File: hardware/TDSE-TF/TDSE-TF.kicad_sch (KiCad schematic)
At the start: 38 parts, among them J1 Sensor nivel de agua, J10 CN10, J11 220VCA salida, J2 Tira LED, J3 +5VCC entrada, J4 220VCA entrada, J5 Bomba, J6 Sensor nivel de luz, J7 Conector LCD16x02, J8 Sensor humedad de suelo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

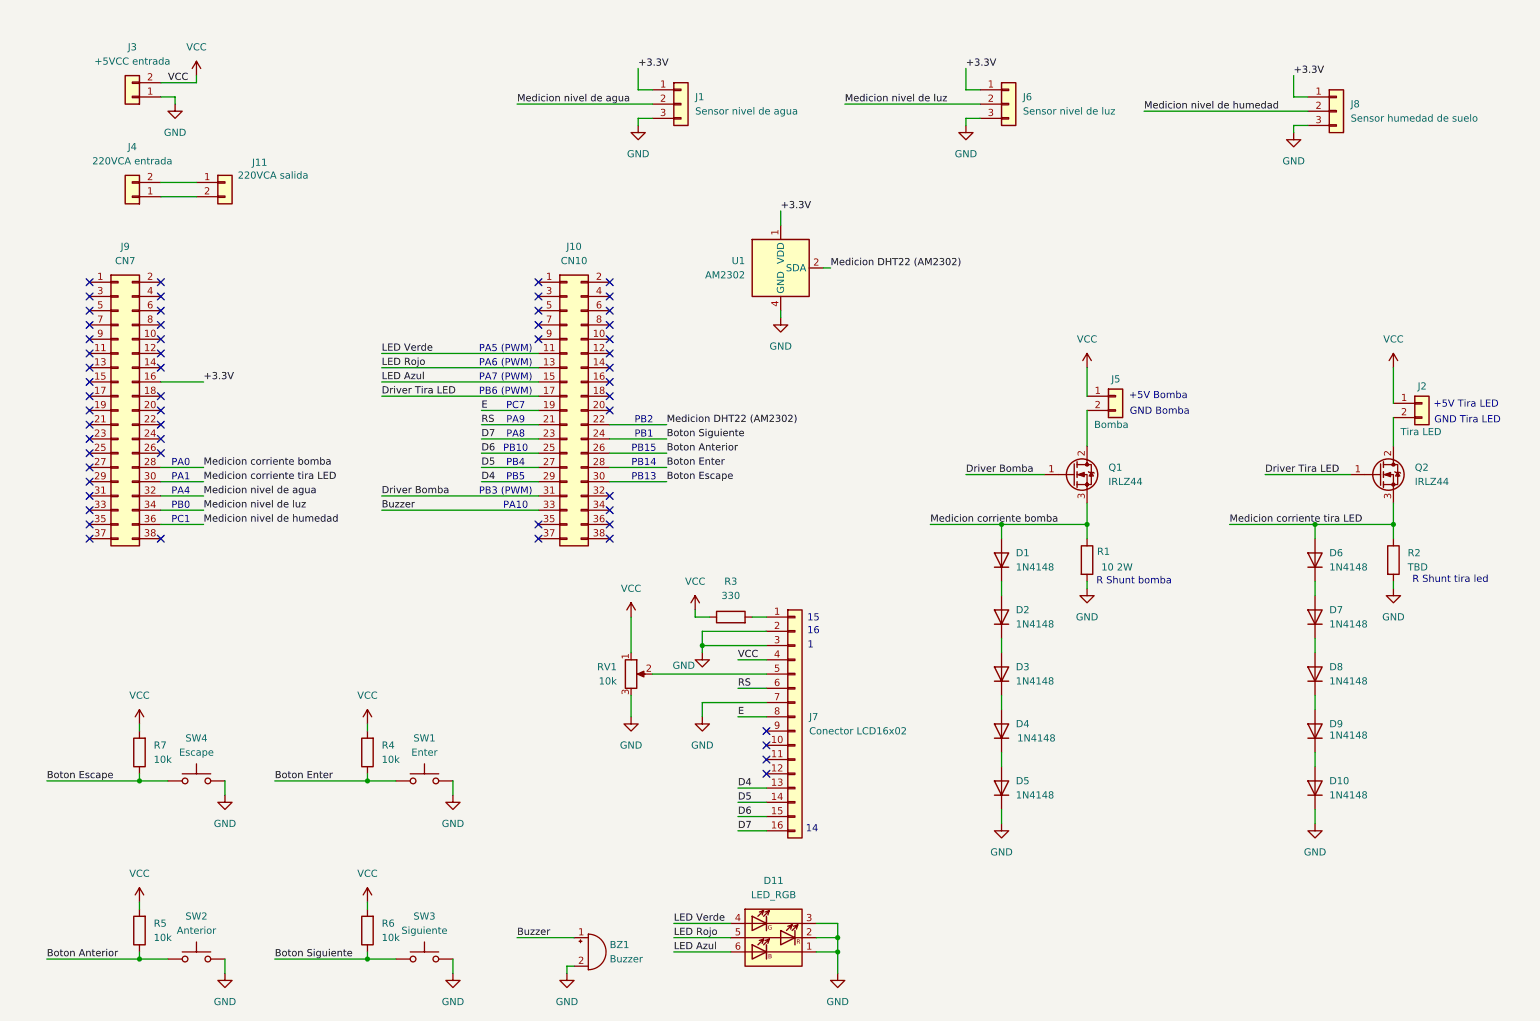
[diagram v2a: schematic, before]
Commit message: Finalizados esquema y placa
Se completó el diseño del circuito esquemático y de la placa asociada al proyecto.
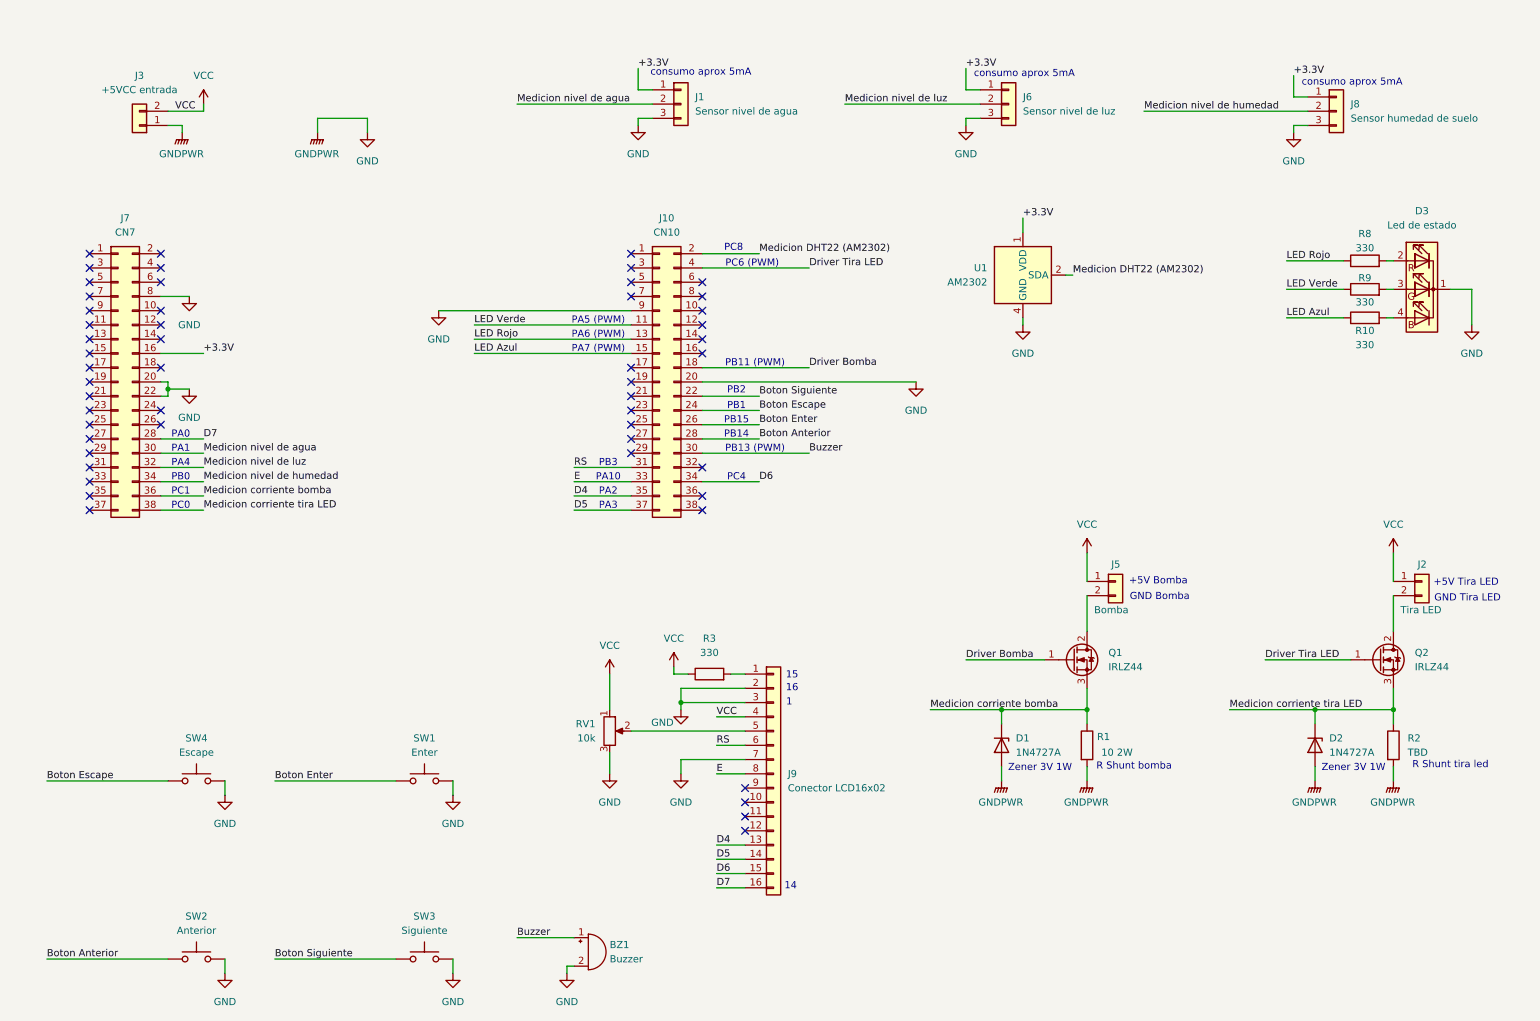
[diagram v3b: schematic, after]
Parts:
- removed D1, D10, D2, D3, D4, D5, D6, D7, D8, D9: 1N4148, Diode_THT:D_DO-35_SOD27_P7.62mm_Horizontal, symbol Diode:1N4148
- removed D11: LED_RGB, LED_SMD:LED_Inolux_IN-P55TATRGB_PLCC6_5.0x5.5mm_P1.8mm, symbol LED:Inolux_IN-P55TATRGB
- removed J11: 220VCA salida, symbol Connector_Generic:Conn_01x02
- removed J4: 220VCA entrada, symbol Connector_Generic:Conn_01x02
- removed R4, R5, R6, R7: 10k, symbol Device:R
- added D1, D2: 1N4727A, Diode_THT:D_DO-41_SOD81_P10.16mm_Horizontal, symbol Diode:1N47xxA
- added D3: Led de estado, LED_THT:LED_D5.0mm-4_RGB_Wide_Pins, symbol Device:LED_KRGB
- added R10, R8, R9: 330, Resistor_THT:R_Axial_DIN0207_L6.3mm_D2.5mm_P7.62mm_Horizontal, symbol Device:R
- BZ1: footprint (none) -> Buzzer_Beeper:Buzzer_12x9.5RM7.6
- J1, J6, J8: footprint (none) -> Connector_PinHeader_2.54mm:PinHeader_1x03_P2.54mm_Vertical
- J10: footprint (none) -> Connector_PinSocket_2.54mm:PinSocket_2x19_P2.54mm_Vertical
- J2, J3, J5: footprint (none) -> Connector_PinHeader_2.54mm:PinHeader_1x02_P2.54mm_Vertical
- J7: renamed from J9; footprint (none) -> Connector_PinSocket_2.54mm:PinSocket_2x19_P2.54mm_Vertical
- J9: renamed from J7; footprint (none) -> Connector_PinSocket_2.54mm:PinSocket_1x16_P2.54mm_Vertical
- R2: footprint (none) -> Resistor_THT:R_Axial_DIN0617_L17.0mm_D6.0mm_P25.40mm_Horizontal
- R3: footprint (none) -> Resistor_THT:R_Axial_DIN0207_L6.3mm_D2.5mm_P7.62mm_Horizontal
- RV1: footprint (none) -> Potentiometer_THT:Potentiometer_Bourns_3386C_Horizontal
- SW1, SW2, SW3, SW4: footprint (none) -> TerminalBlock:TerminalBlock_MaiXu_MX126-5.0-02P_1x02_P5.00mm
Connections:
- net Boton Anterior: now also J10.28 (Pin_28); no longer J10.26 (Pin_26)
- net Boton Enter: now also J10.26 (Pin_26); no longer J10.28 (Pin_28)
- net Boton Escape: now also J10.24 (Pin_24); no longer J10.30 (Pin_30)
- net Boton Siguiente: now also J10.22 (Pin_22); no longer J10.24 (Pin_24)
- net Buzzer: now also J10.30 (Pin_30); no longer J10.33 (Pin_33)
- net D4: now also J10.35 (Pin_35); no longer J10.29 (Pin_29)
- net D5: now also J10.37 (Pin_37); no longer J10.27 (Pin_27)
- net D6: now also J10.34 (Pin_34); no longer J10.25 (Pin_25)
- net D7: now also J7.28 (Pin_28); no longer J10.23 (Pin_23)
- net Driver Bomba: now also J10.18 (Pin_18); no longer J10.31 (Pin_31)
- net Driver Tira LED: now also J10.4 (Pin_4); no longer J10.17 (Pin_17)
- net E: now also J10.33 (Pin_33); no longer J10.19 (Pin_19)
- net GND: now also J10.20 (Pin_20), J10.9 (Pin_9), J7.20 (Pin_20), J7.22 (Pin_22), J7.8 (Pin_8), D1.2 (A), D2.2 (A), D3.1 (K)
- net LED Azul: now also R10.1
- net LED Rojo: now also R8.1
- net LED Verde: now also R9.1
- net Medicion DHT22 (AM2302): now also J10.2 (Pin_2); no longer J10.22 (Pin_22)
- net Medicion corriente bomba: now also J7.36 (Pin_36), D1.1 (K); no longer J7.28 (Pin_28)
- net Medicion corriente tira LED: now also J7.38 (Pin_38), D2.1 (K); no longer J7.30 (Pin_30)
- net Medicion nivel de agua: now also J7.30 (Pin_30); no longer J7.32 (Pin_32)
- net Medicion nivel de humedad: now also J7.34 (Pin_34); no longer J7.36 (Pin_36)
- net Medicion nivel de luz: now also J7.32 (Pin_32); no longer J7.34 (Pin_34)
- net RS: now also J10.31 (Pin_31); no longer J10.21 (Pin_21)
- new net: D3.2 (RA), R8.2
- new net: D3.3 (GA), R9.2
- new net: D3.4 (BA), R10.2
- no-connect marks 57 -> 52
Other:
- note added: "PA2"
- note added: "PA3"
- note added: "PB11 (PWM)"
- note added: "PB13 (PWM)"
- note added: "PB3"
- note added: "PC0"
- note added: "PC4"
- note added: "PC6 (PWM)"
- note added: "PC8"
- note added: "Zener 3V 1W"
- note added: "consumo aprox 5mA"
- note removed: "PA8"
- note removed: "PA9"
- note removed: "PB10"
- note removed: "PB13"
- note removed: "PB3 (PWM)"
- note removed: "PB4"
- note removed: "PB5"
- note removed: "PB6 (PWM)"
- note removed: "PC7"
- moved on the sheet: J10, J2, J3, J5, J7, J9, Q1, Q2, R1, R2, R3, RV1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

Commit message: Circuito final - Rev2
Revisión 2 del circuito esquemático y del PCB.
Cambios en conexiones del LCD.
Ajustes de Capa FFab.
Adjunto nota sobre configuración de jumpres y orden de conexionado de la placa.
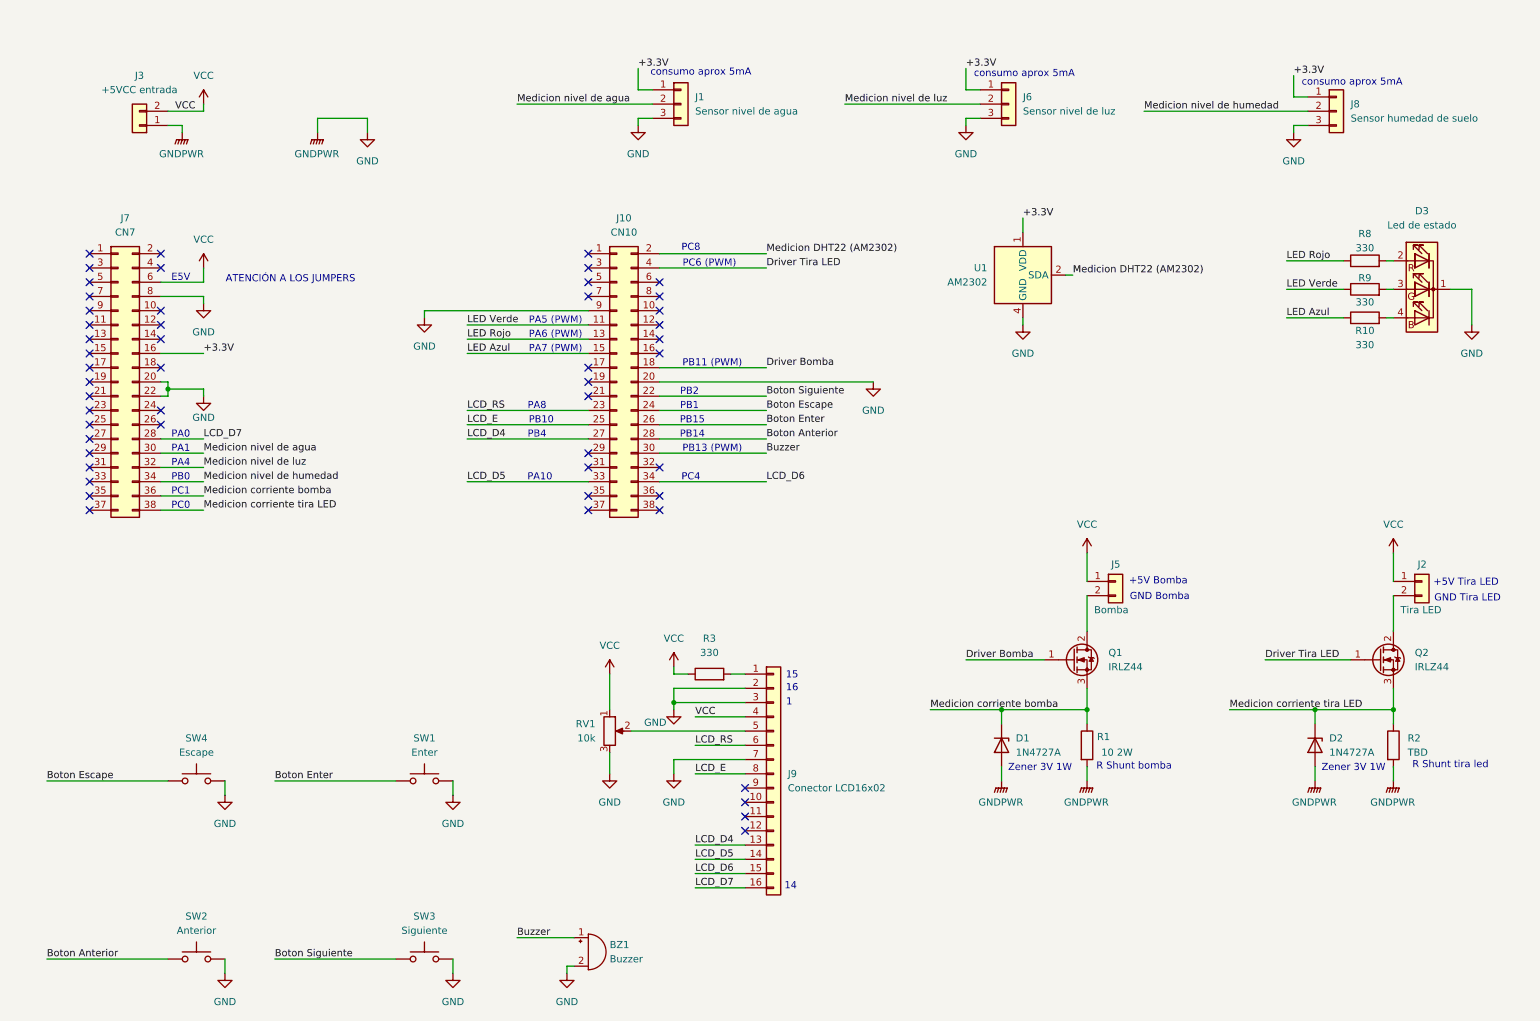
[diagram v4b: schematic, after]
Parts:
- SW1, SW2, SW3, SW4: footprint TerminalBlock:TerminalBlock_MaiXu_MX126-5.0-02P_1x02_P5.00mm -> Button_Switch_THT:SW_PUSH_1P1T 2 pines
- U1: footprint Sensor:ASAIR_AM2302_P2.54mm_Vertical -> Connector_PinSocket_2.54mm:PinSocket_1x04_P2.54mm_Vertical
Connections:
- net VCC: now also J7.6 (Pin_6)
- net LCD_RS: now reaches J10.23 (Pin_23)
- net LCD_RS: now also J9.6 (Pin_6)
- net LCD_E: now reaches J10.25 (Pin_25)
- net LCD_E: now also J9.8 (Pin_8)
- net LCD_D4: now reaches J10.27 (Pin_27)
- net LCD_D4: now also J9.13 (Pin_13)
- net D4: no longer names the net of J10.35 (Pin_35)
- net D4: no longer J9.13 (Pin_13)
- net D5: no longer names the net of J10.37 (Pin_37)
- net D5: no longer J9.14 (Pin_14)
- net D6 renamed LCD_D6
- net D7 renamed LCD_D7
- net E renamed LCD_D5
- net LCD_D5: now also J9.14 (Pin_14); no longer J9.8 (Pin_8)
- net RS: no longer names the net of J10.31 (Pin_31)
- net RS: no longer J9.6 (Pin_6)
- no-connect marks 52 -> 51
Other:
- note added: "ATENCIÓN A LOS JUMPERS"
- note added: "E5V"
- note added: "PA8"
- note added: "PB10"
- note added: "PB4"
- note removed: "PA2"
- note removed: "PA3"
- note removed: "PB3"
- moved on the sheet: J10

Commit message: PCB final Rev 2
Corregido conexionado de LCD.
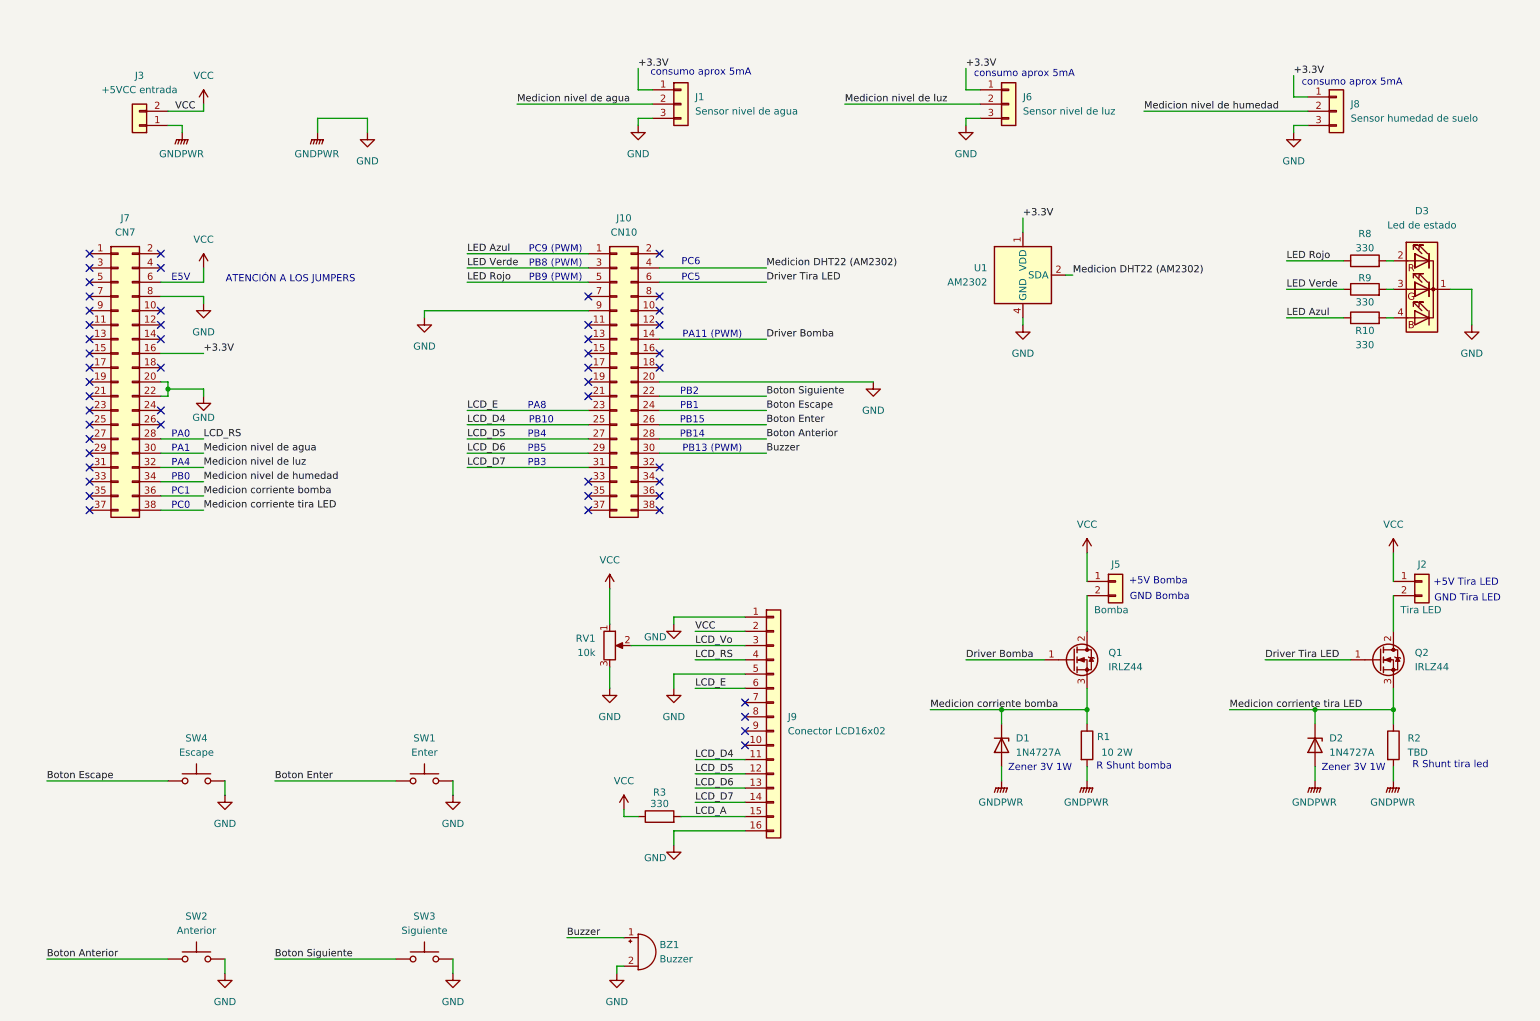
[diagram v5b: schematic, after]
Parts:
- R3: footprint Resistor_THT:R_Axial_DIN0207_L6.3mm_D2.5mm_P7.62mm_Horizontal -> Resistor_THT:R_Axial_DIN0207_L6.3mm_D2.5mm_P15.24mm_Horizontal
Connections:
- net Driver Bomba: now also J10.14 (Pin_14); no longer J10.18 (Pin_18)
- net Driver Tira LED: now also J10.6 (Pin_6); no longer J10.4 (Pin_4)
- net GND: now also J9.1 (Pin_1), J9.16 (Pin_16), J9.5 (Pin_5); no longer J9.2 (Pin_2), J9.3 (Pin_3), J9.7 (Pin_7)
- net LCD_D4: now also J10.25 (Pin_25), J9.11 (Pin_11); no longer J10.27 (Pin_27), J9.13 (Pin_13)
- net LCD_D5: now also J10.27 (Pin_27), J9.12 (Pin_12); no longer J10.33 (Pin_33), J9.14 (Pin_14)
- net LCD_D6: now also J10.29 (Pin_29), J9.13 (Pin_13); no longer J10.34 (Pin_34), J9.15 (Pin_15)
- net LCD_D7: now also J10.31 (Pin_31), J9.14 (Pin_14); no longer J7.28 (Pin_28), J9.16 (Pin_16)
- net LCD_E: now also J10.23 (Pin_23), J9.6 (Pin_6); no longer J10.25 (Pin_25), J9.8 (Pin_8)
- net LCD_RS: now also J7.28 (Pin_28), J9.4 (Pin_4); no longer J10.23 (Pin_23), J9.6 (Pin_6)
- net LED Azul: now also J10.1 (Pin_1); no longer J10.15 (Pin_15)
- net LED Rojo: now also J10.5 (Pin_5); no longer J10.13 (Pin_13)
- net LED Verde: now also J10.3 (Pin_3); no longer J10.11 (Pin_11)
- net Medicion DHT22 (AM2302): now also J10.4 (Pin_4); no longer J10.2 (Pin_2)
- net VCC: now also J9.2 (Pin_2); no longer J9.4 (Pin_4)
- net LCD_A: now reaches R3.2
- net LCD_A: now also J9.15 (Pin_15); no longer J9.1 (Pin_1)
- net LCD_Vo: now reaches RV1.2
- net LCD_Vo: now also J9.3 (Pin_3); no longer J9.5 (Pin_5)
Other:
- note added: "PA11 (PWM)"
- note added: "PB3"
- note added: "PB5"
- note added: "PB8 (PWM)"
- note added: "PB9 (PWM)"
- note added: "PC5"
- note added: "PC6"
- note added: "PC9 (PWM)"
- note removed: "1"
- note removed: "14"
- note removed: "15"
- note removed: "16"
- note removed: "PA10"
- note removed: "PA5 (PWM)"
- note removed: "PA6 (PWM)"
- note removed: "PA7 (PWM)"
- note removed: "PB11 (PWM)"
- note removed: "PC4"
- note removed: "PC6 (PWM)"
- note removed: "PC8"
- moved on the sheet: BZ1, J9, R3, RV1
